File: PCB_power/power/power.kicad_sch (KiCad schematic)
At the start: 18 parts, among them J1 Conn_01x02_Pin, J2 Conn_01x02_Pin, J3 Conn_01x02_Pin, U1 BQ21040DBV, U2 TLV61048, U3 MCP1825S

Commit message: started layout placement
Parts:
- L2: renamed from L1; footprint SmartPaper:SDES064T-100MS -> Library:SDES064T-100MS
- renumbered C1 to C18, C2 to C19, C3 to C20, C4 to C21, D1 to D4, D2 to D5, J2 to J3, J1 to J4, J3 to J5, R5 to R10, R6 to R11, R1 to R7, R2 to R8, R3 to R9, U1 to U4, U2 to U5, U3 to U6

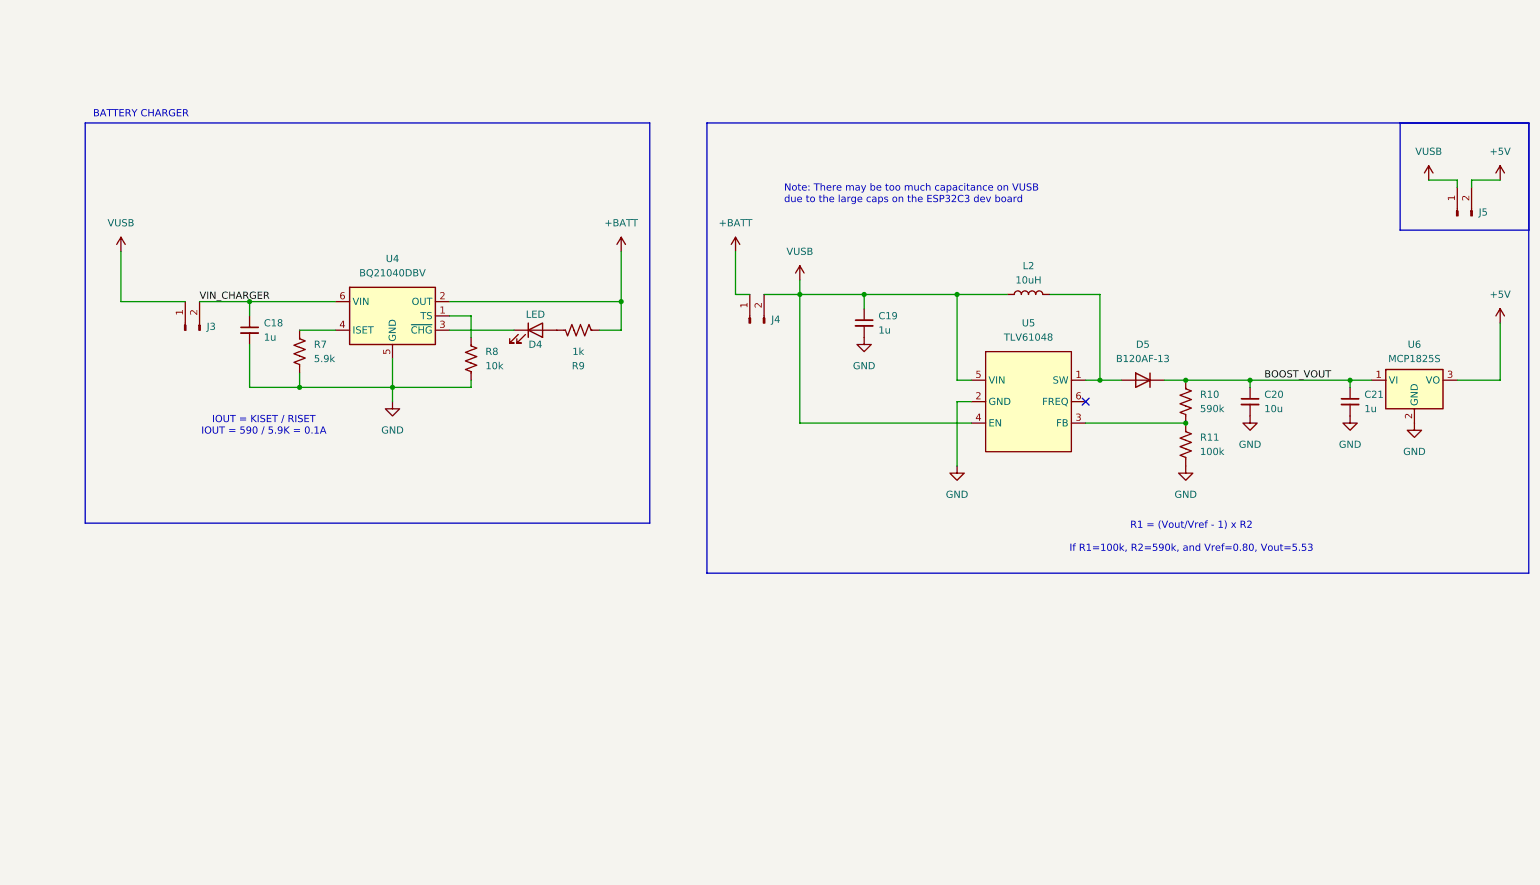
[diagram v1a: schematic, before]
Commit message: updated power circuitry
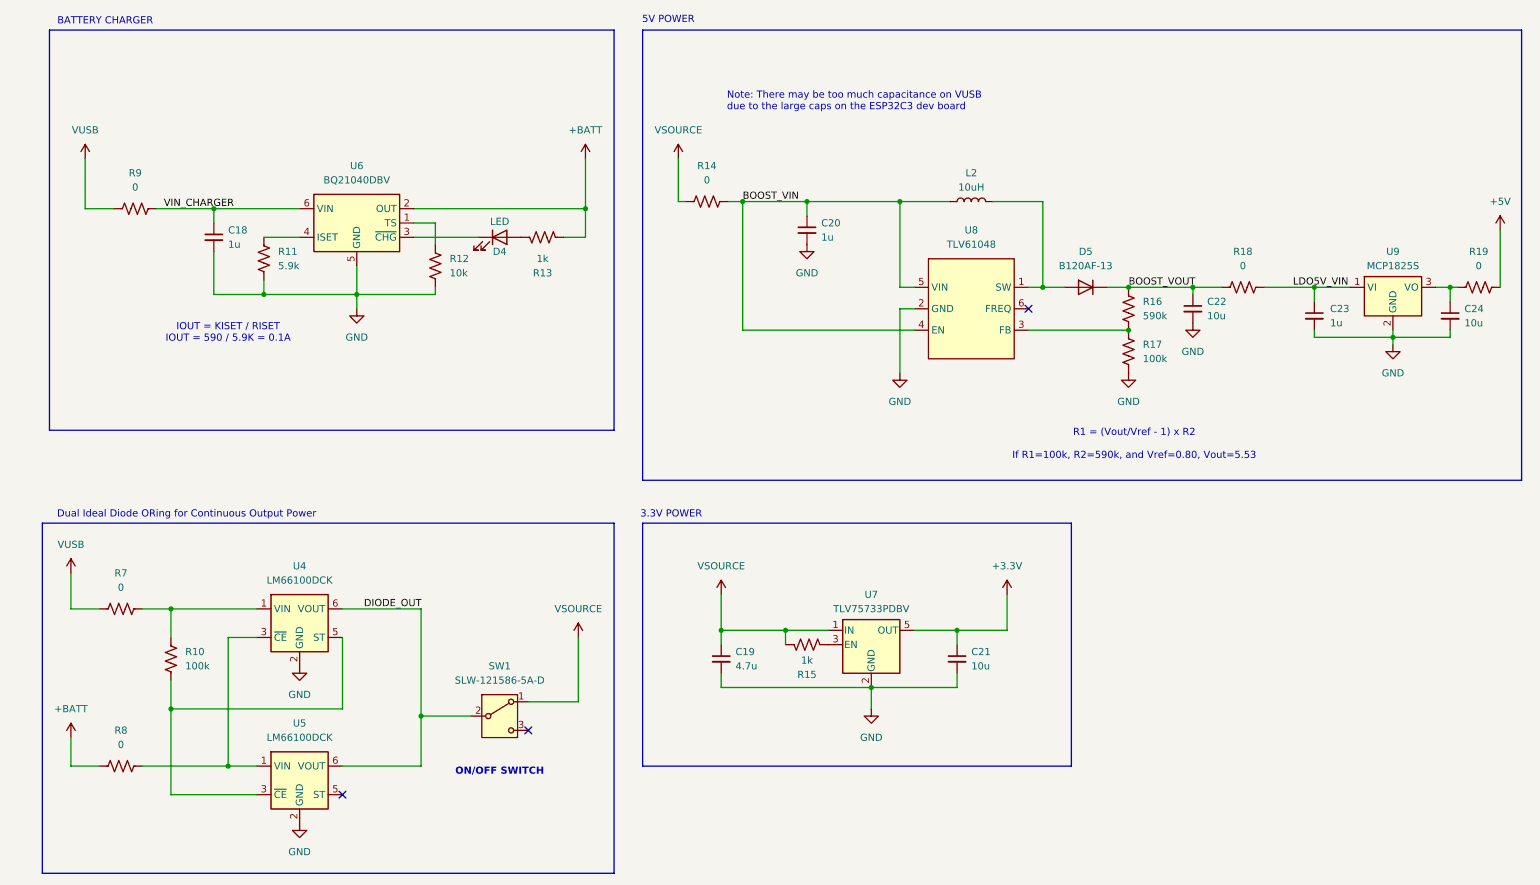
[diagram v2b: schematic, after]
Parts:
- removed J3, J4, J5: Conn_01x02_Pin, Connector_PinHeader_1.00mm:PinHeader_1x02_P1.00mm_Vertical, symbol Connector:Conn_01x02_Pin
- added C19: 4.7u, Capacitor_SMD:C_0805_2012Metric_Pad1.18x1.45mm_HandSolder, symbol Device:C_Small
- added C21, C24: 10u, Capacitor_SMD:C_0805_2012Metric_Pad1.18x1.45mm_HandSolder, symbol Device:C_Small
- added R10: 100k, Resistor_SMD:R_0805_2012Metric_Pad1.20x1.40mm_HandSolder, symbol Device:R_US
- added R14, R18, R19, R7, R8, R9: 0, Resistor_SMD:R_0805_2012Metric_Pad1.20x1.40mm_HandSolder, symbol Device:R_US
- added R15: 1k, Resistor_SMD:R_0805_2012Metric_Pad1.20x1.40mm_HandSolder, symbol Device:R_US
- added SW1: SLW-121586-5A-D, Library:SW_SLW-121586-5A-D, symbol SymbolLibrary:SLW-121586-5A-D
- added U4, U5: LM66100DCK, Package_TO_SOT_SMD:SOT-363_SC-70-6, symbol Power_Management:LM66100DCK
- added U7: TLV75733PDBV, Package_TO_SOT_SMD:SOT-23-5, symbol Regulator_Linear:TLV75733PDBV
- renumbered C19 to C20, C20 to C22, C21 to C23, R7 to R11, R8 to R12, R9 to R13, R10 to R16, R11 to R17, U4 to U6, U5 to U8, U6 to U9
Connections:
- net +5V: now also R19.2; no longer U9.3 (VO)
- net +BATT: now also R8.1
- net BOOST_VOUT: now also R18.1; no longer C23.1, U9.1 (VI)
- net GND: now also C19.2, C21.2, C24.2, U4.2 (GND), U5.2 (GND), U7.2 (GND)
- net VIN_CHARGER: now also R9.2
- net VUSB: now also R7.1, R9.1; no longer C20.1, L2.1, U8.4 (EN), U8.5 (VIN)
- new net: R15.2, U7.3 (EN)
- new net: R10.2, R7.2, U4.1 (VIN)
- new net: C24.1, R19.1, U9.3 (VO)
- new net: R8.2, U4.3 (~{CE}), U5.1 (VIN)
- new net: R10.1, U4.5 (ST), U5.3 (~{CE})
- new net +3.3V: C21.1, U7.5 (OUT)
- new net BOOST_VIN: C20.1, L2.1, R14.2, U8.4 (EN), U8.5 (VIN)
- new net DIODE_OUT: SW1.2 (B), U4.6 (VOUT), U5.6 (VOUT)
- new net LDO5V_VIN: C23.1, R18.2, U9.1 (VI)
- new net VSOURCE: C19.1, R14.1, R15.1, SW1.1 (A), U7.1 (IN)
- no-connect marks 1 -> 3
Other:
- note added: "3.3V POWER"
- note added: "5V POWER"
- note added: "Dual Ideal Diode ORing for Continuous Output Power"
- note added: "ON/OFF SWITCH"
- moved on the sheet: C18, C20, C22, C23, D4, D5, L2, R11, R12, R13, R16, R17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

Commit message: power nets
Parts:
- removed R10: 100k, Resistor_SMD:R_0805_2012Metric_Pad1.20x1.40mm_HandSolder, symbol Device:R_US
- added C19: 10u, Capacitor_SMD:C_0805_2012Metric_Pad1.18x1.45mm_HandSolder, symbol Device:C_Small
- L2: value 10uH -> 3.3 uH; footprint Library:SDES064T-100MS -> Library:IND_VLS6045AF-3R3N
- R10: renamed from R11; value 5.9k -> 5.36k
- renumbered C19 to C20, C20 to C21, C21 to C22, C22 to C23, C23 to C24, C24 to C25, R12 to R11, R13 to R12, R14 to R13, R15 to R14, R16 to R15, R17 to R16, R18 to R17, R19 to R18
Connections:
- net +BATT: now also C19.1
- net GND: now also U8.6 (FREQ), C19.2
- net at R7.2, U4.1 (VIN): now also U5.3 (~{CE})
- net at U4.5 (ST): no longer U5.3 (~{CE})
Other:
- note added: "5V LDO"
- note added: "BOOST CONVERTER"
- note added: "DESIGN ASSUMES 3.3V LDO IS UNSOLDERED FROM THE ESP32C3 BOARD"
- note added: "Dual Ideal Diode ORing"
- note added: "FREQ = GND for 1 MHz switching frequency. Higher switching frequency improves load transient response but reduces efficiency slightly. The other benefit of higher switching frequency is lower output ripple voltage."
- note added: "IOUT = KISET / RISET IOUT = 540 / 5.36k = 0.1A"
- note added: "R1 = (Vout/Vref - 1) x R2 If R1(top)=590k, R2(bottom)=100k, and Vref=0.80, Vout=5.53"
- note added: "To Disable the temp sense function, use a fixed 10k resistor between the TS (terminal 1) and Vss"
- note removed: "5V POWER"
- note removed: "Dual Ideal Diode ORing for Continuous Output Power"
- note removed: "IOUT = KISET / RISET IOUT = 590 / 5.9K = 0.1A"
- note removed: "Note: There may be too much capacitance on VUSB due to the large caps on the ESP32C3 dev board"
- note removed: "R1 = (Vout/Vref - 1) x R2 If R1=100k, R2=590k, and Vref=0.80, Vout=5.53"
- moved on the sheet: C21, R17
